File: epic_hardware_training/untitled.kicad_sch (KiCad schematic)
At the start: 7 parts, among them U2 OKI

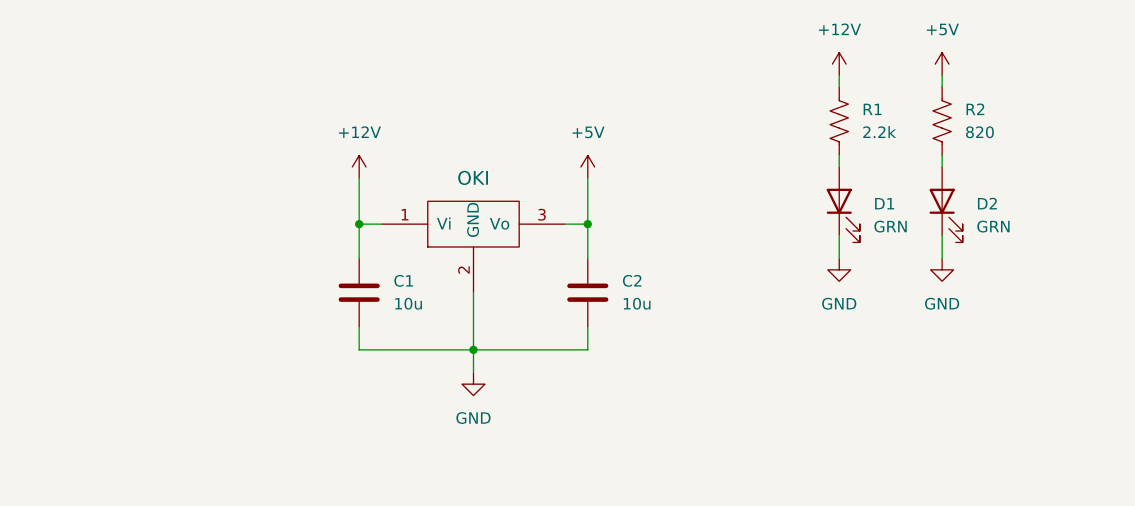
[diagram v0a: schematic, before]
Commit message: complete schematic
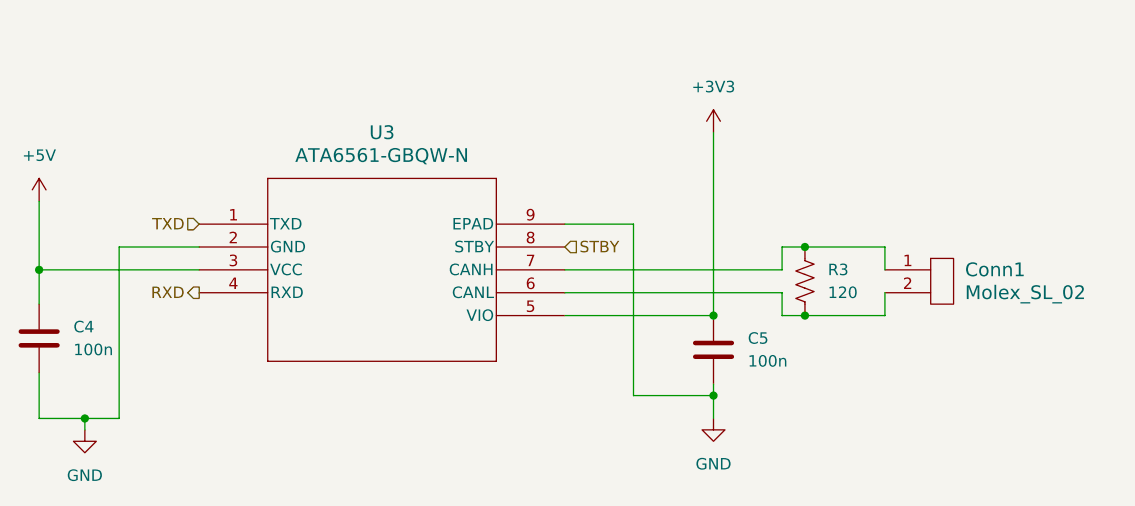
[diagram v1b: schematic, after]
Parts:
- removed C1, C2: 10u, symbol Device:C
- removed D1, D2: GRN, symbol Device:LED
- removed R1: 2.2k, symbol Device:R_US
- removed R2: 820, symbol Device:R_US
- removed U2: OKI, symbol MRDT_Devices:OKI
- added C4, C5: 100n, symbol Device:C
- added Conn1: Molex_SL_02, symbol MRDT_Connectors:Molex_SL_02
- added R3: 120, symbol Device:R_US
- added U3: ATA6561-GBQW-N, VDFN8_3X3_MCH, symbol 2026_Training_Hardware:ATA6561-GBQW-N
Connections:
- net +5V: now also C4.1, U3.3 (VCC)
- net GND: now also C4.2, C5.2, U3.2 (GND), U3.9 (EPAD)
- new net: Conn1.1, R3.1, U3.7 (CANH)
- new net: Conn1.2, R3.2, U3.6 (CANL)
- new net +3V3: C5.1, U3.5 (VIO)
- new net RXD: U3.4 (RXD)
- new net STBY: U3.8 (STBY)
- new net TXD: U3.1 (TXD)
